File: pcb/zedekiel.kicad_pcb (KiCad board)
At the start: 2 copper layers, 304 x 95 mm, 179 parts, among them K1 KEYSW, K10 KEYSW, K11 KEYSW, K12 KEYSW, K13 KEYSW, K14 KEYSW, K15 KEYSW, K16 KEYSW, K17 KEYSW, K18 KEYSW, K19 KEYSW, K2 KEYSW, K20 KEYSW, K21 KEYSW, K22 KEYSW, K23 KEYSW, K24 KEYSW, K25 KEYSW, K26 KEYSW, K27 KEYSW, K28 KEYSW, K29 KEYSW, K3 KEYSW, K30 KEYSW, K31 KEYSW, K32 KEYSW, K33 KEYSW, K34 KEYSW, K35 KEYSW, K36 KEYSW, K37 KEYSW, K38 KEYSW, K39 KEYSW, K4 KEYSW, K40 KEYSW, K41 KEYSW, K42 KEYSW, K43 KEYSW, K44 KEYSW, K45 KEYSW, K46 KEYSW, K47 KEYSW, K48 KEYSW, K49 KEYSW, K5 KEYSW, K50 KEYSW, K51 KEYSW, K52 KEYSW, K53 KEYSW, K54 KEYSW, K55 KEYSW, K56 KEYSW, K57 KEYSW, K58 KEYSW, K59 KEYSW, K6 KEYSW, K60 KEYSW, K61 KEYSW, K62 KEYSW, K63 KEYSW, K64 KEYSW, K65 KEYSW, K66 KEYSW, K7 KEYSW, K8 KEYSW, K9 KEYSW, SW1 SW_PUSH, U1 ATmega16U4-AU_(modified), X1 16MHz

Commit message: progress on the case
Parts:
- K1, K43, K56, K66: footprint custom:Kailh_socket_MX_with_switch_1.00U -> custom:Kailh_socket_MX_with_switch_1.50U
- K15: footprint custom:Kailh_socket_MX_with_switch_1.00U -> custom:Kailh_socket_MX_with_switch_1.75U
- K28, K60: footprint custom:Kailh_socket_MX_with_switch_1.00U -> custom:Kailh_socket_MX_with_switch_2.25U
- K29, K42, K55, K57, K64: footprint custom:Kailh_socket_MX_with_switch_1.00U -> custom:Kailh_socket_MX_with_switch_2.00U
- K58, K61, K62, K63, K65: footprint custom:Kailh_socket_MX_with_switch_1.00U -> custom:Kailh_socket_MX_with_switch_1.25U

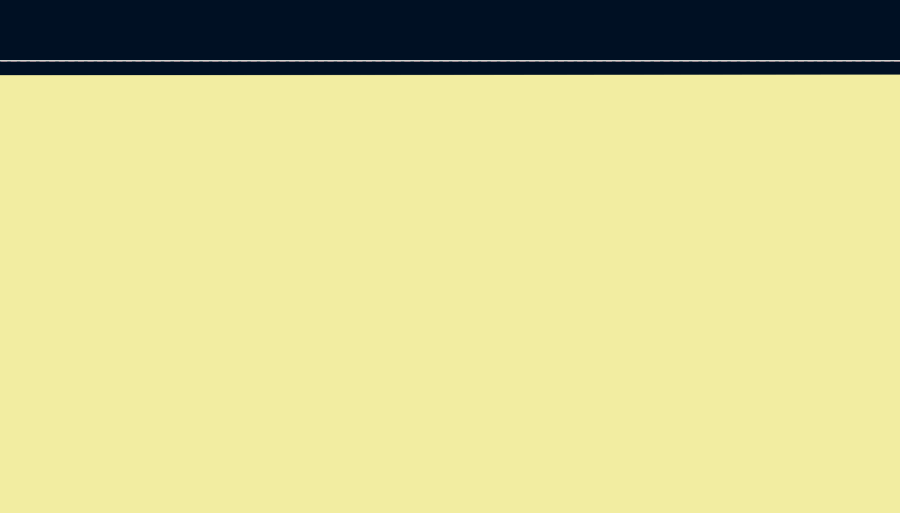
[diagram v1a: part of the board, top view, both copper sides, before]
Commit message: finished the case, minor change on pcb
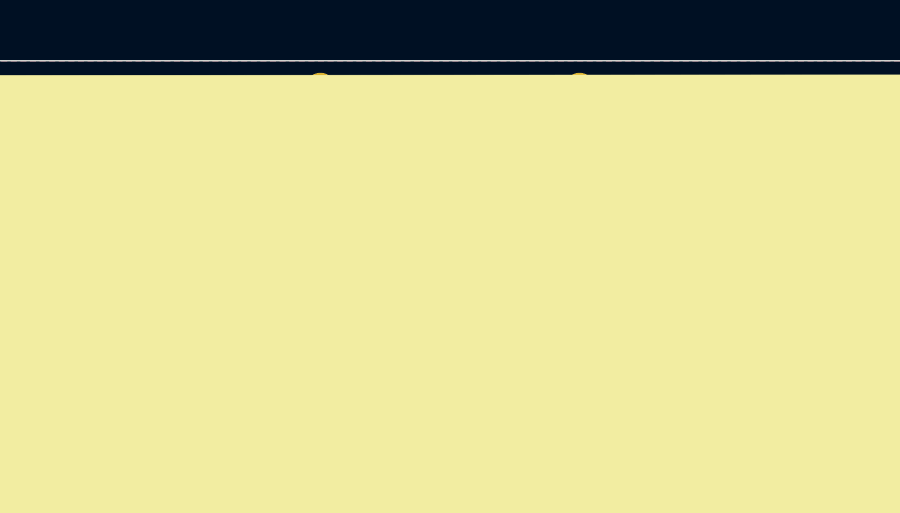
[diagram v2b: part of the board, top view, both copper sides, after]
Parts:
- moved USB1 0.40 mm to (47.6, 19.0)
